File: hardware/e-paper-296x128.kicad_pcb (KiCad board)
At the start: 2 copper layers, 95 x 40 mm, 49 parts, among them P1 CON-SENSOR, P4 BOOT, P5 DEBUG, Q1 2N7002P, U1 XMC1404, U2 Con24HT, U4 DRILL, U5 DRILL, U6 DRILL, U7 DRILL

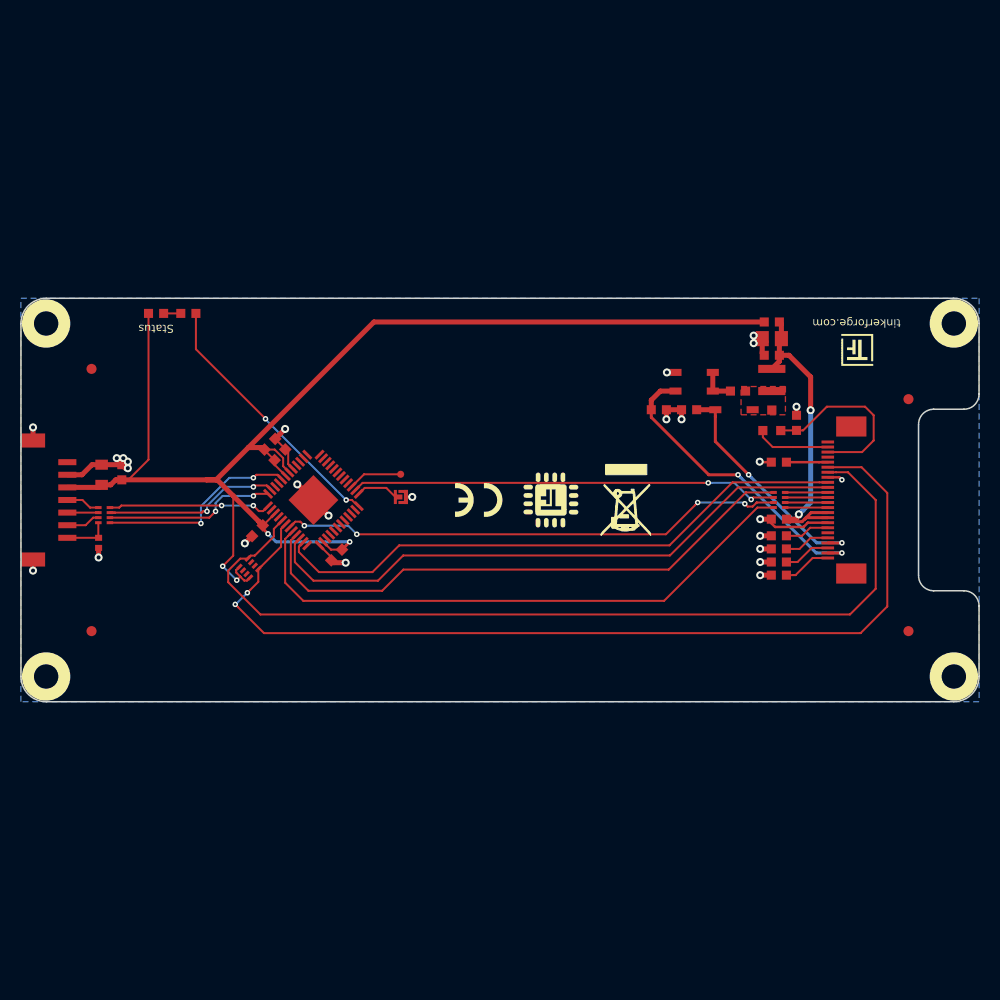
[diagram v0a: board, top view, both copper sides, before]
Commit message: New standart layout. Switched to Kicad 6
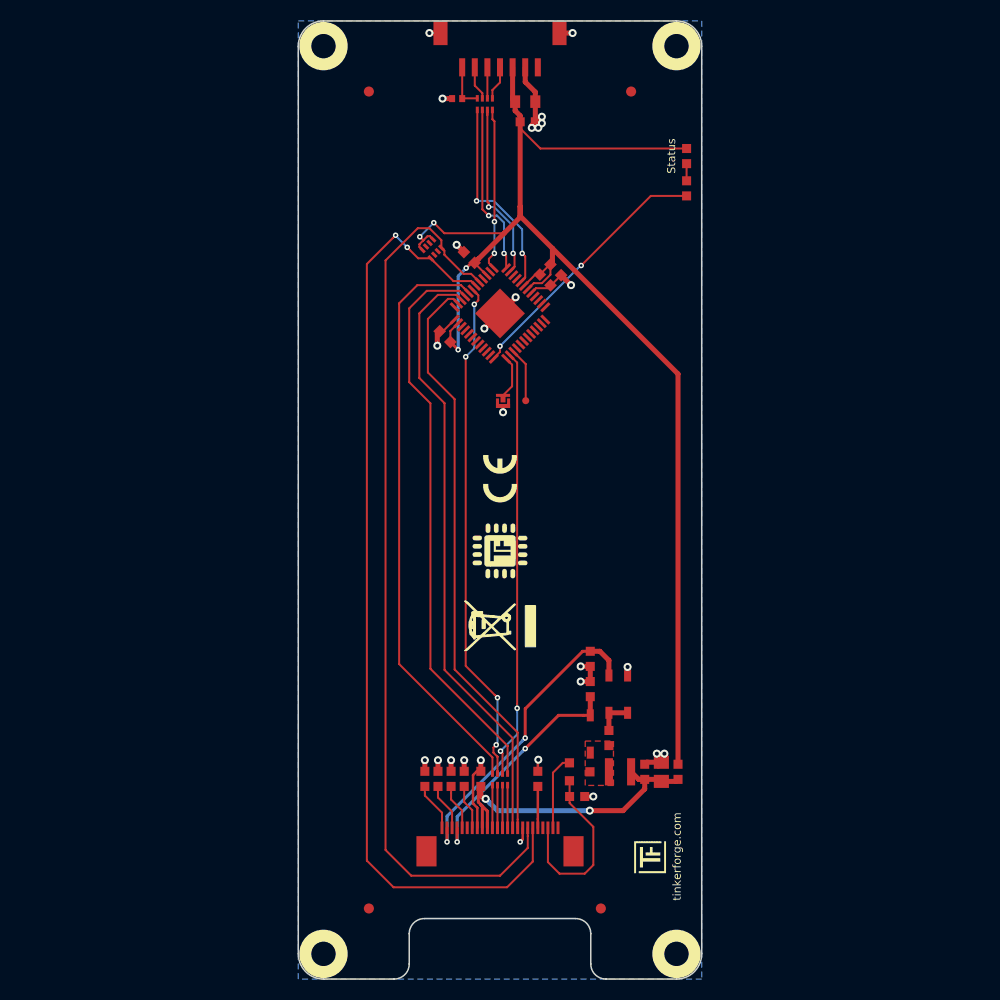
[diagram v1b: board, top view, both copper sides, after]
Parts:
- moved U4 68.3 mm to (133.0, 150.0), turned to -90 degrees
- moved U5 68.3 mm to (168.0, 150.0), turned to -90 degrees
- moved U6 68.3 mm to (133.0, 60.0), turned to -90 degrees
- moved U7 68.3 mm to (168.0, 60.0), turned to -90 degrees
- moved G*** 67.4 mm to (164.1, 150.7), turned to 90 degrees
- moved P1 67.2 mm to (150.5, 57.5), turned to 180 degrees
- moved Fiducial_Mark 60.2 mm to (163.5, 64.5), turned to -90 degrees
- moved Fiducial_Mark 60.2 mm to (137.5, 64.5), turned to -90 degrees
- moved Fiducial_Mark 60.2 mm to (137.5, 145.5), turned to -90 degrees
- moved Fiducial_Mark 59.0 mm to (160.5, 145.5), turned to -90 degrees
- moved C1 56.6 mm to (146.2, 65.2), turned to 0 degrees
- moved C3 56.0 mm to (153.0, 65.5), turned to 180 degrees
- moved G*** 55.6 mm to (163.8, 142.0), turned to 90 degrees
- moved RP1 55.5 mm to (149.0, 65.8), turned to 180 degrees
- moved D1 54.9 mm to (169.0, 70.9), turned to -90 degrees
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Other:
- board size 95 x 40 mm -> 40 x 95 mm
- net class Default removed
- board text added: "Copyright Tinkerforge GmbH 2018. This documentation describes Open Hardware and is licensed under the CERN OHL v. 1.1. You may redistribute and modify this documentation under the terms of the CERN OHL v.1.1. (http://ohwr.org/cernohl). This documentation is distributed WITHOUT ANY EXPRESS OR IMPLIED WARRANTY, INCLUDING OF MERCHANTABILITY, SATISFACTORY QUALITY AND FITNESS FOR A PARTICULAR PURPOSE.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"
